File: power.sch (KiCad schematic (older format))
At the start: 17 parts

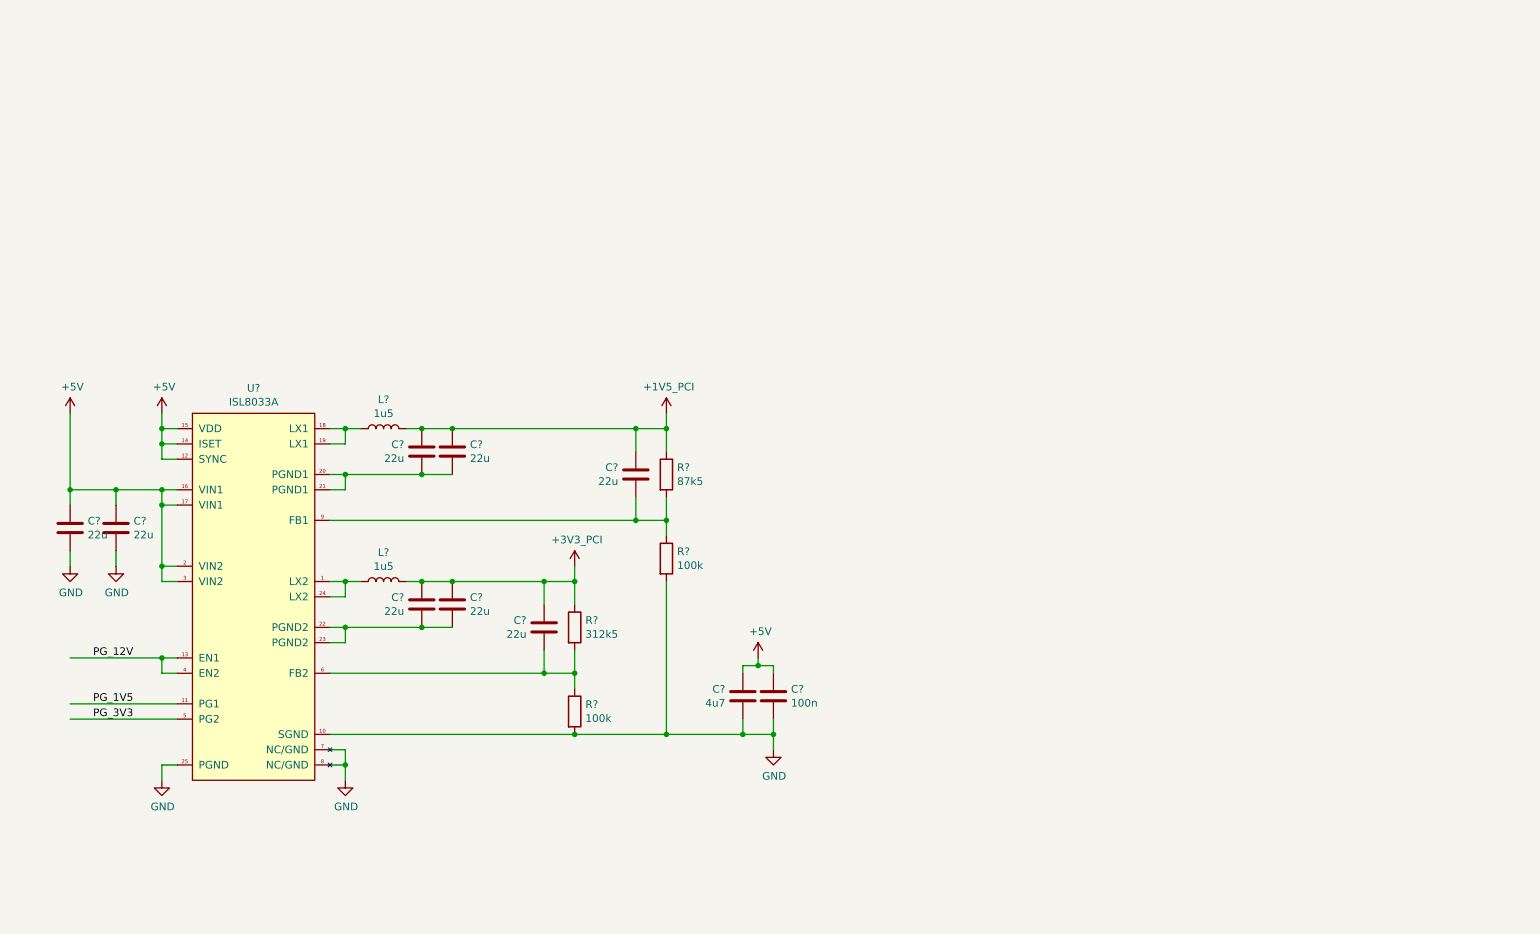
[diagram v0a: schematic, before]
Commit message: sch: Add 5V PSU
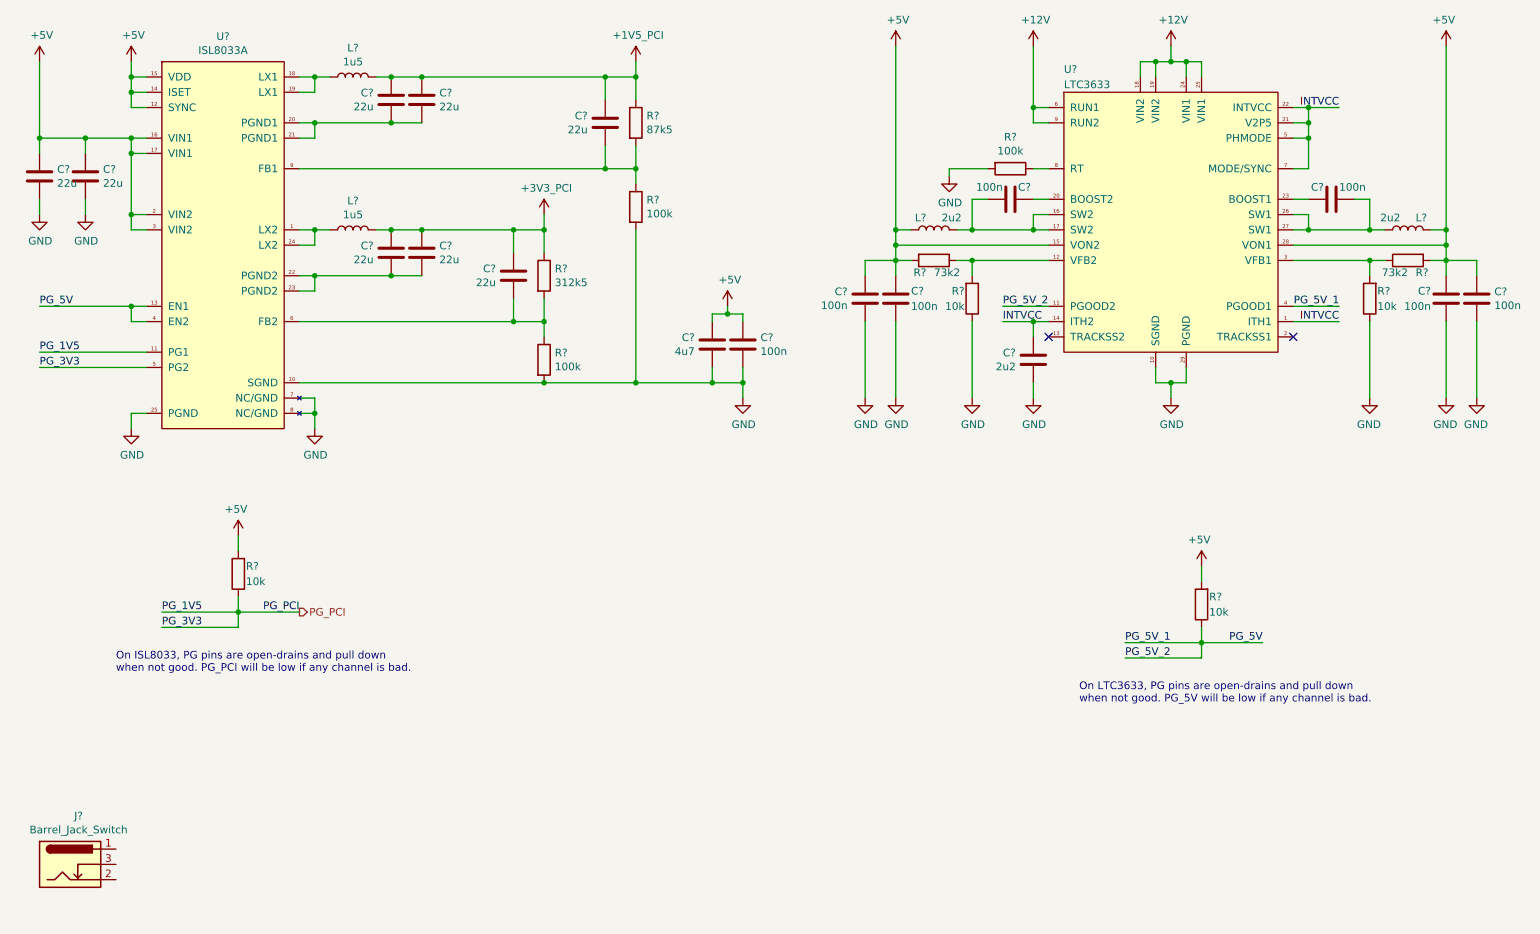
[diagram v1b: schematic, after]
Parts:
- added C? (x6): 100n, symbol Device:C
- added C?: 2u2, symbol Device:C
- added J?: Barrel_Jack_Switch, symbol Connector:Barrel_Jack_Switch
- added L? (x2): 2u2, symbol Device:L
- added R?: 100k, symbol Device:R
- added R? (x2): 73k2, symbol Device:R
- added R? (x4): 10k, symbol Device:R
- added U?: LTC3633, Package_DFN_QFN:QFN-28-1EP_4x5mm_P0.5mm_EP2.65x3.65mm_ThermalVias, symbol pimouss-motherboard:LTC3633
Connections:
- net labels added: +12V, INTVCC, PG_5V, PG_5V_1, PG_5V_2, PG_PCI
- net labels removed: PG_12V
- wire segments 87 -> 181
- no-connect marks 0 -> 2
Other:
- note added: "On ISL8033, PG pins are open-drains and pull down\nwhen not good. PG_PCI will be low if any channel is bad.\n"
- note added: "On LTC3633, PG pins are open-drains and pull down\nwhen not good. PG_5V will be low if any channel is bad.\n"
- moved on the sheet: C?, L?, R?, U?

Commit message: sch: Add main power input
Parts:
- added C?: CP_Small, symbol Device:CP_Small
- added Q?: DMP2040USS, Package_SO:SOIC-8_3.9x4.9mm_P1.27mm, symbol pimouss-motherboard:DMP2040USS
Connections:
- net +12V: now also C?.1, Q?.1 (S), Q?.2 (S), Q?.3 (S)
- net GND: now also J?.2, J?.3, C?.2, Q?.4 (G)
- net at J?.1: now also Q?.5 (D), Q?.6 (D), Q?.7 (D), Q?.8 (D)
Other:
- moved on the sheet: J?
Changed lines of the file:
@@
 L Connector:Barrel_Jack_Switch J?
 U 1 1 5D2C9CDF
-P 1400 6950
-F 0 "J?" H 1455 7267 50  0000 C CNN
-F 1 "Barrel_Jack_Switch" H 1455 7176 50  0000 C CNN
-F 2 "" H 1450 6910 50  0001 C CNN
-F 3 "~" H 1450 6910 50  0001 C CNN
-	1    1400 6950
+P 2700 6800
+F 0 "J?" H 2755 7117 50  0000 C CNN
+F 1 "Barrel_Jack_Switch" H 2755 7026 50  0000 C CNN
+F 2 "" H 2750 6760 50  0001 C CNN
+F 3 "~" H 2750 6760 50  0001 C CNN
+	1    2700 6800
 	1    0    0    -1
 $EndComp
+$Comp
+L power:GND #PWR?
+U 1 1 5D2D1D48
+P 3100 7100
+F 0 "#PWR?" H 3100 6850 50  0001 C CNN
+F 1 "GND" H 3105 6927 50  0000 C CNN
+F 2 "" H 3100 7100 50  0001 C CNN
+F 3 "" H 3100 7100 50  0001 C CNN
+	1    3100 7100
+	1    0    0    -1
+$EndComp
+Wire Wire Line
+	3000 6900 3100 6900
+Wire Wire Line
+	3100 6900 3100 7100
+Wire Wire Line
+	3000 6800 3100 6800
+Wire Wire Line
+	3100 6800 3100 6900
+Connection ~ 3100 6900
+$Comp
+L pimouss-motherboard:DMP2040USS Q?
+U 1 1 5D2E0A7B
+P 3700 6800
+F 0 "Q?" V 4043 6800 50  0000 C CNN
+F 1 "DMP2040USS" V 3952 6800 50  0000 C CNN
+F 2 "Package_SO:SOIC-8_3.9x4.9mm_P1.27mm" H 3900 6900 50  0001 C CNN
+F 3 "https://www.diodes.com/assets/Datasheets/DMP2040USS.pdf" H 3700 6800 50  0001 C CNN
+	1    3700 6800
+	0    -1   -1   0
+$EndComp
+Wire Wire Line
+	3000 6700 3500 6700
+$Comp
+L power:GND #PWR?
+U 1 1 5D2EFEF0
+P 3700 7100
+F 0 "#PWR?" H 3700 6850 50  0001 C CNN
+F 1 "GND" H 3705 6927 50  0000 C CNN
+F 2 "" H 3700 7100 50  0001 C CNN
+F 3 "" H 3700 7100 50  0001 C CNN
+	1    3700 7100
+	1    0    0    -1
+$EndComp
+Wire Wire Line
+	3700 7000 3700 7100
+$Comp
+L Device:CP_Small C?
+U 1 1 5D306FC4
+P 4200 6900
+F 0 "C?" H 4288 6946 50  0000 L CNN
+F 1 "CP_Small" H 4288 6855 50  0000 L CNN
+F 2 "" H 4200 6900 50  0001 C CNN
+F 3 "~" H 4200 6900 50  0001 C CNN
+	1    4200 6900
+	1    0    0    -1
+$EndComp
+$Comp
+L power:GND #PWR?
+U 1 1 5D3071B2
+P 4200 7100
+F 0 "#PWR?" H 4200 6850 50  0001 C CNN
+F 1 "GND" H 4205 6927 50  0000 C CNN
+F 2 "" H 4200 7100 50  0001 C CNN
+F 3 "" H 4200 7100 50  0001 C CNN
+	1    4200 7100
+	1    0    0    -1
+$EndComp
+$Comp
+L power:+12V #PWR?
+U 1 1 5D3076B1
+P 4200 6600
+F 0 "#PWR?" H 4200 6450 50  0001 C CNN
+F 1 "+12V" H 4215 6773 50  0000 C CNN
+F 2 "" H 4200 6600 50  0001 C CNN
+F 3 "" H 4200 6600 50  0001 C CNN
+	1    4200 6600
+	1    0    0    -1
+$EndComp
+Wire Wire Line
+	3900 6700 4200 6700
+Wire Wire Line
+	4200 6700 4200 6600
+Wire Wire Line
+	4200 6700 4200 6800
+Connection ~ 4200 6700
+Wire Wire Line
+	4200 7000 4200 7100
 $EndSCHEMATC
